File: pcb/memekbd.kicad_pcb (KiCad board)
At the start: 2 copper layers, 134.1 x 130.9 mm, 194 parts, among them J1 MJ-4PP-9, J2 MJ-4PP-9, SW1 SW_Push, SW10 SW_Push, SW11 SW_Push, SW12 SW_Push, SW13 SW_Push, SW14 SW_Push, SW15 SW_Push, SW16 SW_Push, SW17 SW_Push, SW18 SW_Push, SW19 SW_Push, SW2 SW_Push, SW20 SW_Push, SW21 SW_Push, SW22 SW_Push, SW23 SW_Push, SW24 SW_Push, SW25 SW_Push, SW26 SW_Push, SW27 SW_Push, SW28 SW_Push, SW29 SW_Push, SW3 SW_Push, SW30 SW_Push, SW31 SW_Push, SW32 SW_Push, SW33 SW_Push, SW34 SW_Push, SW35 SW_Push, SW36 SW_Push, SW37 SW_Push, SW38 SW_Push, SW39 SW_Push, SW4 SW_Push, SW40 SW_Push, SW41 SW_Push, SW42 SW_Push, SW43 SW_Push, SW44 SW_Push, SW45 SW_Push, SW46 SW_Push, SW47 SW_Push, SW48 SW_Push, SW5 SW_Push, SW6 SW_Push, SW7 SW_Push, SW8 SW_Push, SW9 SW_Push, U1 ProMicro, U2 ProMicro

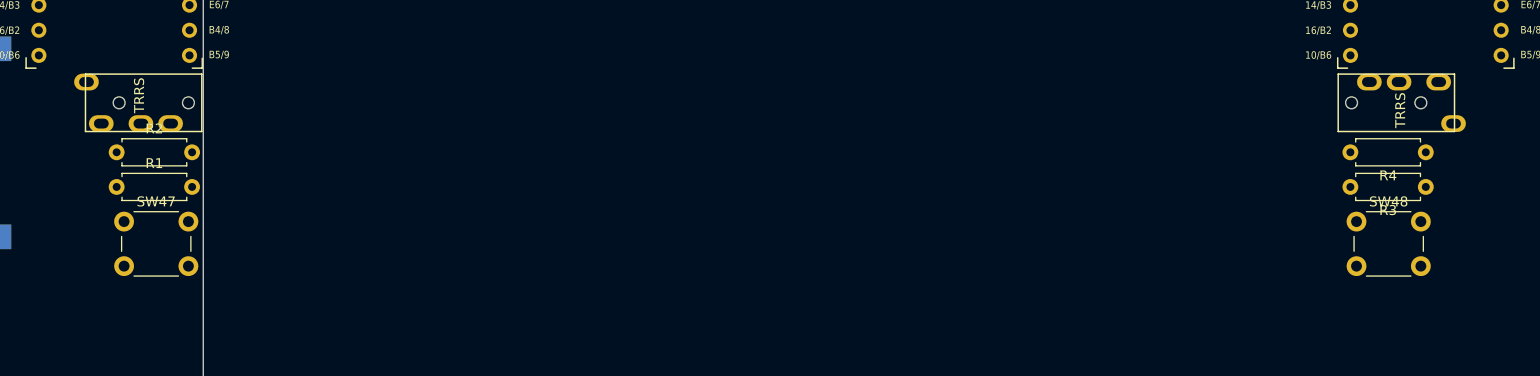
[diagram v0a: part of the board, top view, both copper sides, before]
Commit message: Remove unnecessary libraries. Update footprints
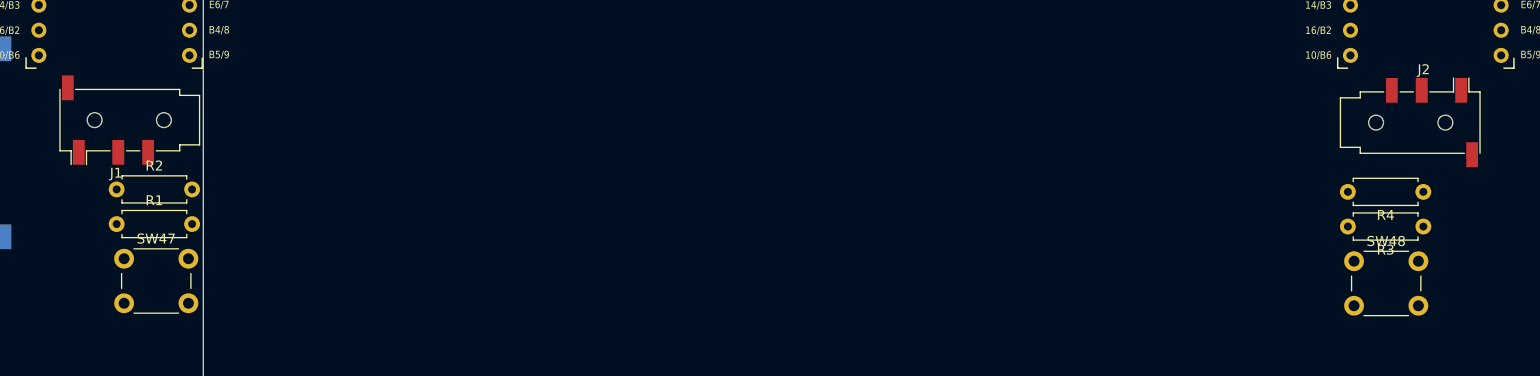
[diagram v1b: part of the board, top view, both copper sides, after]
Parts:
- J1, J2: value MJ-4PP-9 -> AudioJack4; footprint kbd:MJ-4PP-9_1side -> Connector_Audio:Jack_3.5mm_PJ320D_Horizontal
- moved J2 8.98 mm to (255.2, 83.5), turned to 0 degrees
- moved J1 8.92 mm to (123.2, 83.2), turned to 180 degrees
- moved R3 4.01 mm to (255.2, 94.0)
- moved R4 4.01 mm to (255.2, 90.5)
- moved SW48 4.01 mm to (248.2, 97.5)
- moved R1 3.75 mm to (123.2, 93.8)
- moved R2 3.75 mm to (123.2, 90.2)
- moved SW47 3.75 mm to (124.0, 97.2)

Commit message: Add mounting holes.
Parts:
- added REF**: MountingHole_5.3mm_M5_ISO7380, MountingHole:MountingHole_5.3mm_M5_ISO7380, F.Cu at (101.2, 39.8)
- added REF**: MountingHole_3.2mm_M3_ISO7380, MountingHole:MountingHole_3.2mm_M3_ISO7380, F.Cu at (38.5, 59.0)
- added REF**: MountingHole_3.2mm_M3_ISO7380, MountingHole:MountingHole_3.2mm_M3_ISO7380, F.Cu at (136.5, 122.8)
- added REF**: MountingHole_3.2mm_M3_ISO7380, MountingHole:MountingHole_3.2mm_M3_ISO7380, F.Cu at (94.8, 64.0)
- added REF**: MountingHole_5.3mm_M5_ISO7380, MountingHole:MountingHole_5.3mm_M5_ISO7380, F.Cu at (126.5, 105.2)
- added REF**: MountingHole_5.3mm_M5_ISO7380, MountingHole:MountingHole_5.3mm_M5_ISO7380, F.Cu at (28.0, 46.8)
- added REF**: MountingHole_5.3mm_M5_ISO7380, MountingHole:MountingHole_5.3mm_M5_ISO7380, F.Cu at (43.2, 105.2)
- added REF**: MountingHole_3.2mm_M3_ISO7380, MountingHole:MountingHole_3.2mm_M3_ISO7380, F.Cu at (74.0, 122.2)
- added REF**: MountingHole_3.2mm_M3_ISO7380, MountingHole:MountingHole_3.2mm_M3_ISO7380, F.Cu at (94.8, 102.0)
- added REF**: MountingHole_3.2mm_M3_ISO7380, MountingHole:MountingHole_3.2mm_M3_ISO7380, F.Cu at (75.0, 76.0)
- added REF**: MountingHole_3.2mm_M3_ISO7380, MountingHole:MountingHole_3.2mm_M3_ISO7380, F.Cu at (75.0, 38.0)
- added REF**: MountingHole_3.2mm_M3_ISO7380, MountingHole:MountingHole_3.2mm_M3_ISO7380, F.Cu at (36.8, 29.2)
- added REF**: MountingHole_3.2mm_M3_ISO7380, MountingHole:MountingHole_3.2mm_M3_ISO7380, F.Cu at (37.0, 90.0)
- moved SW48 10.0 mm to (258.2, 97.0), turned to 90 degrees
- moved SW47 8.27 mm to (115.8, 96.8), turned to 90 degrees
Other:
- outline, holes or cut-outs redrawn

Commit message: Some routing
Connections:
- J1 pad R1: /lSCL -> /lSDA
- J1 pad R2: /lSDA -> /lSCL
- J2 pad R1: /rSCL -> /rSDA
- J2 pad R2: /rSDA -> /rSCL
- R1 pad 1: /lSDA -> /lSCL
- R2 pad 1: /lSCL -> /lSDA
- R3 pad 1: /rSDA -> /rSCL
- R4 pad 1: /rSCL -> /rSDA
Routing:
- net GND: track 0.00 -> 452.3 mm, vias 0 -> 1
- net +5V: track 0.00 -> 194.4 mm
- net /lrow4: track 0.00 -> 133.9 mm
- net /lrow3: track 0.00 -> 124.7 mm
- net /lcol3: track 0.00 -> 121.1 mm, vias 0 -> 2
- net /lrow2: track 0.00 -> 106.6 mm
- net /lcol1: track 0.00 -> 94.1 mm
- net /lrow1: track 0.00 -> 93.4 mm
- net /lrow0: track 0.00 -> 75.2 mm
- net /lcol2: track 0.00 -> 70.0 mm
- net /lcol0: track 0.00 -> 59.2 mm
- net /lcol4: track 0.00 -> 38.0 mm
- net Net-(D4-Pad2): track 0.00 -> 4.40 mm
- net Net-(D14-Pad2): track 0.00 -> 4.36 mm
- net Net-(D8-Pad2): track 0.00 -> 4.34 mm
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
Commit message: Some LED changes.
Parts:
- added R5: 1k, Resistor_THT:R_Axial_DIN0207_L6.3mm_D2.5mm_P7.62mm_Horizontal, F.Cu at (96.2, 29.0)
- added R6: 1k, Resistor_THT:R_Axial_DIN0207_L6.3mm_D2.5mm_P7.62mm_Horizontal, F.Cu at (282.2, 29.0)
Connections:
- LED15 pad 2: Net-(LED1-Pad4) -> Net-(LED15-Pad2)
- LED20 pad 2: Net-(LED2-Pad4) -> Net-(LED20-Pad2)
- LED21 pad 2: Net-(LED21-Pad2) -> Net-(LED20-Pad2)
- LED23 pad 2: Net-(LED23-Pad2) -> Net-(LED22-Pad2)
- LED25 pad 4: Net-(LED25-Pad4) -> Net-(LED24-Pad4)
- LED27 pad 4: Net-(LED27-Pad4) -> Net-(LED26-Pad4)
- LED28 pad 4: /rLED -> Net-(LED28-Pad4)
- LED3 pad 4: Net-(LED21-Pad2) -> Net-(LED2-Pad4)
- LED38 pad 2: Net-(LED24-Pad4) -> Net-(LED38-Pad2)
- LED4 pad 4: Net-(LED22-Pad2) -> Net-(LED4-Pad4)
- LED43 pad 2: Net-(LED25-Pad4) -> Net-(LED38-Pad2)
- LED44 pad 2: Net-(LED26-Pad4) -> Net-(LED44-Pad2)
- LED45 pad 2: Net-(LED27-Pad4) -> Net-(LED44-Pad2)
- LED5 pad 4: /lLED -> Net-(LED1-Pad4)
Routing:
- net (no net): vias 43 -> 42

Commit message: Routing progress
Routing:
- net +5V: track 194.4 -> 758.4 mm
- net GND: track 452.3 -> 661.4 mm
- net /lrow4: track 133.9 -> 86.6 mm
- net /lRST: track 0.00 -> 43.6 mm
- net Net-(LED1-Pad4): track 0.00 -> 42.0 mm, vias 0 -> 2
- net /lLED: track 0.00 -> 40.9 mm
- net /lSCL: track 0.00 -> 35.3 mm
- net /lcol1: track 94.1 -> 59.3 mm
- net /lSDA: track 0.00 -> 34.4 mm
- net /lcol0: track 59.2 -> 82.0 mm
- net Net-(LED14-Pad2): track 0.00 -> 21.4 mm, vias 0 -> 2
- net /lcol4: track 38.0 -> 58.1 mm, vias 0 -> 1
- net Net-(LED3-Pad2): track 0.00 -> 19.2 mm, vias 0 -> 2
- net Net-(LED4-Pad2): track 0.00 -> 18.9 mm, vias 0 -> 2
- net Net-(LED19-Pad2): track 0.00 -> 18.3 mm, vias 0 -> 2
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
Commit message: Routing progress
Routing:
- net /lcol1: track 59.3 -> 194.1 mm, vias 0 -> 6
- net /lcol0: track 82.0 -> 182.5 mm, vias 0 -> 3
- net /lcol2: track 70.0 -> 167.2 mm, vias 0 -> 3
- net /lcol4: track 58.1 -> 121.8 mm, vias 1 -> 3
- net /lRST: track 43.6 -> 19.8 mm
- net +5V: track 758.4 -> 773.8 mm
- net GND: track 661.4 -> 650.6 mm

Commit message: Routing progress
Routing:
- net Net-(LED22-Pad2): track 0.00 -> 66.9 mm, vias 0 -> 2
- net /lcol3: track 123.4 -> 166.8 mm
- net Net-(LED2-Pad4): track 0.00 -> 23.0 mm, vias 0 -> 2
- net /lcol4: track 121.8 -> 138.4 mm
- net +5V: track 773.8 -> 785.9 mm
- net GND: track 650.6 -> 662.5 mm
- net /lrow3: vias 0 -> 1
- net (no net): vias 4 -> 0
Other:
- outline, holes or cut-outs redrawn

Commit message: Routing progress
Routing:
- net /lrow4: track 86.6 -> 134.9 mm, vias 0 -> 2
- net /lRST: track 19.8 -> 44.9 mm
- net Net-(LED22-Pad2): track 66.9 -> 70.6 mm
- net +5V: track 785.9 -> 785.0 mm
- net /lcol3: track 166.8 -> 167.5 mm
- net /lcol4: vias 3 -> 2
